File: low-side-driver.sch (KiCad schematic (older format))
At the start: 4 parts, among them U2 74HC595

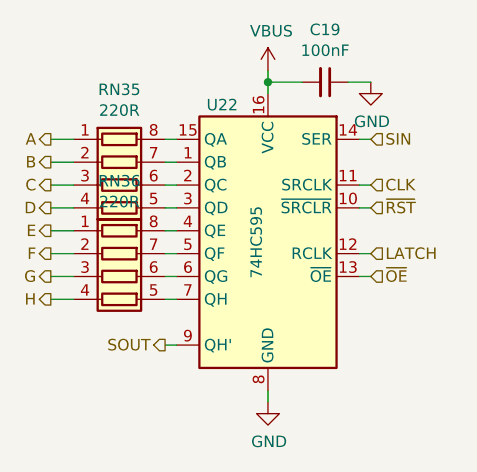
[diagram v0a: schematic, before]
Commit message: Use better ESP32 Pico D4 footprint
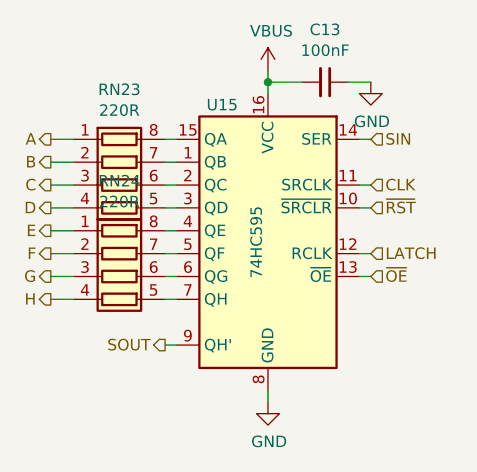
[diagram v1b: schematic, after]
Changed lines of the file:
@@
 $Descr A4 11693 8268
 encoding utf-8
-Sheet 5 25
+Sheet 16 25
 Title ""
 Date ""
@@
 AR Path="/61C4C905/61A75B6D/61A5FAFA" Ref="#PWR0153"  Part="1"
 AR Path="/61C4C905/61A75B93/61A5FAFA" Ref="#PWR0156"  Part="1"
-F 0 "#PWR0156" H 4900 3900 50  0001 C CNN
+F 0 "#PWR0138" H 4900 3900 50  0001 C CNN
 F 1 "GND" H 4905 3977 50  0000 C CNN
 F 2 "" H 4900 4150 50  0001 C CNN
@@
 AR Path="/61C4C905/61A75B6D/61A64A59" Ref="#PWR0154"  Part="1"
 AR Path="/61C4C905/61A75B93/61A64A59" Ref="#PWR0157"  Part="1"
-F 0 "#PWR0157" H 5350 2500 50  0001 C CNN
+F 0 "#PWR0139" H 5350 2500 50  0001 C CNN
 F 1 "GND" H 5355 2577 50  0000 C CNN
 F 2 "" H 5350 2750 50  0001 C CNN
@@
 AR Path="/61C4C905/61A75B6D/61A63F1A" Ref="C18"  Part="1"
 AR Path="/61C4C905/61A75B93/61A63F1A" Ref="C19"  Part="1"
-F 0 "C19" V 4921 2750 50  0000 C CNN
+F 0 "C13" V 4921 2750 50  0000 C CNN
 F 1 "100nF" V 5012 2750 50  0000 C CNN
 F 2 "Capacitor_SMD:C_0402_1005Metric" H 5150 2750 50  0001 C CNN
@@
 AR Path="/61C4C905/61A75B6D/61A5EC64" Ref="#PWR0155"  Part="1"
 AR Path="/61C4C905/61A75B93/61A5EC64" Ref="#PWR0158"  Part="1"
-F 0 "#PWR0158" H 4900 2550 50  0001 C CNN
+F 0 "#PWR0140" H 4900 2550 50  0001 C CNN
 F 1 "VBUS" H 4915 2873 50  0000 C CNN
 F 2 "" H 4900 2700 50  0001 C CNN
@@
 AR Path="/61C4C905/61A75B6D/61A5E6B7" Ref="RN34"  Part="1"
 AR Path="/61C4C905/61A75B93/61A5E6B7" Ref="RN36"  Part="1"
-F 0 "RN36" V 3833 3600 50  0000 C CNN
+F 0 "RN24" V 3833 3600 50  0000 C CNN
 F 1 "220R" V 3924 3600 50  0000 C CNN
 F 2 "Resistor_SMD:R_Array_Concave_4x0402" V 4525 3600 50  0001 C CNN
@@
 AR Path="/61C4C905/61A75B6D/61A5E6AC" Ref="RN33"  Part="1"
 AR Path="/61C4C905/61A75B93/61A5E6AC" Ref="RN35"  Part="1"
-F 0 "RN35" V 3833 3200 50  0000 C CNN
+F 0 "RN23" V 3833 3200 50  0000 C CNN
 F 1 "220R" V 3924 3200 50  0000 C CNN
 F 2 "Resistor_SMD:R_Array_Concave_4x0402" V 4525 3200 50  0001 C CNN
@@
 AR Path="/61C4C905/61A75B6D/61A5E6A5" Ref="U21"  Part="1"
 AR Path="/61C4C905/61A75B93/61A5E6A5" Ref="U22"  Part="1"
-F 0 "U22" H 5100 3950 50  0000 C CNN
+F 0 "U15" H 5100 3950 50  0000 C CNN
 F 1 "74HC595" V 4950 3350 50  0000 C CNN
 F 2 "Package_Texas:X1QFN-16-2.5x2.5-EP-1.2" H 4900 3400 50  0001 C CNN

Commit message: Add additional VBUS bulk capacitance
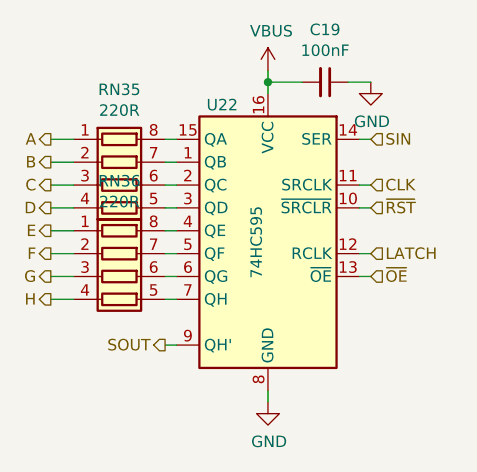
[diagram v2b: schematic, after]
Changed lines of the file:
@@
 $Descr A4 11693 8268
 encoding utf-8
-Sheet 16 25
+Sheet 21 25
 Title ""
 Date ""
@@
 AR Path="/61C4C905/61A75B6D/61A5FAFA" Ref="#PWR0153"  Part="1"
 AR Path="/61C4C905/61A75B93/61A5FAFA" Ref="#PWR0156"  Part="1"
-F 0 "#PWR0138" H 4900 3900 50  0001 C CNN
+F 0 "#PWR0156" H 4900 3900 50  0001 C CNN
 F 1 "GND" H 4905 3977 50  0000 C CNN
 F 2 "" H 4900 4150 50  0001 C CNN
@@
 AR Path="/61C4C905/61A75B6D/61A64A59" Ref="#PWR0154"  Part="1"
 AR Path="/61C4C905/61A75B93/61A64A59" Ref="#PWR0157"  Part="1"
-F 0 "#PWR0139" H 5350 2500 50  0001 C CNN
+F 0 "#PWR0157" H 5350 2500 50  0001 C CNN
 F 1 "GND" H 5355 2577 50  0000 C CNN
 F 2 "" H 5350 2750 50  0001 C CNN
@@
 AR Path="/61C4C905/61A75B6D/61A63F1A" Ref="C18"  Part="1"
 AR Path="/61C4C905/61A75B93/61A63F1A" Ref="C19"  Part="1"
-F 0 "C13" V 4921 2750 50  0000 C CNN
+F 0 "C19" V 4921 2750 50  0000 C CNN
 F 1 "100nF" V 5012 2750 50  0000 C CNN
 F 2 "Capacitor_SMD:C_0402_1005Metric" H 5150 2750 50  0001 C CNN
@@
 AR Path="/61C4C905/61A75B6D/61A5EC64" Ref="#PWR0155"  Part="1"
 AR Path="/61C4C905/61A75B93/61A5EC64" Ref="#PWR0158"  Part="1"
-F 0 "#PWR0140" H 4900 2550 50  0001 C CNN
+F 0 "#PWR0158" H 4900 2550 50  0001 C CNN
 F 1 "VBUS" H 4915 2873 50  0000 C CNN
 F 2 "" H 4900 2700 50  0001 C CNN
@@
 AR Path="/61C4C905/61A75B6D/61A5E6B7" Ref="RN34"  Part="1"
 AR Path="/61C4C905/61A75B93/61A5E6B7" Ref="RN36"  Part="1"
-F 0 "RN24" V 3833 3600 50  0000 C CNN
+F 0 "RN36" V 3833 3600 50  0000 C CNN
 F 1 "220R" V 3924 3600 50  0000 C CNN
 F 2 "Resistor_SMD:R_Array_Concave_4x0402" V 4525 3600 50  0001 C CNN
@@
 AR Path="/61C4C905/61A75B6D/61A5E6AC" Ref="RN33"  Part="1"
 AR Path="/61C4C905/61A75B93/61A5E6AC" Ref="RN35"  Part="1"
-F 0 "RN23" V 3833 3200 50  0000 C CNN
+F 0 "RN35" V 3833 3200 50  0000 C CNN
 F 1 "220R" V 3924 3200 50  0000 C CNN
 F 2 "Resistor_SMD:R_Array_Concave_4x0402" V 4525 3200 50  0001 C CNN
@@
 AR Path="/61C4C905/61A75B6D/61A5E6A5" Ref="U21"  Part="1"
 AR Path="/61C4C905/61A75B93/61A5E6A5" Ref="U22"  Part="1"
-F 0 "U15" H 5100 3950 50  0000 C CNN
+F 0 "U22" H 5100 3950 50  0000 C CNN
 F 1 "74HC595" V 4950 3350 50  0000 C CNN
 F 2 "Package_Texas:X1QFN-16-2.5x2.5-EP-1.2" H 4900 3400 50  0001 C CNN

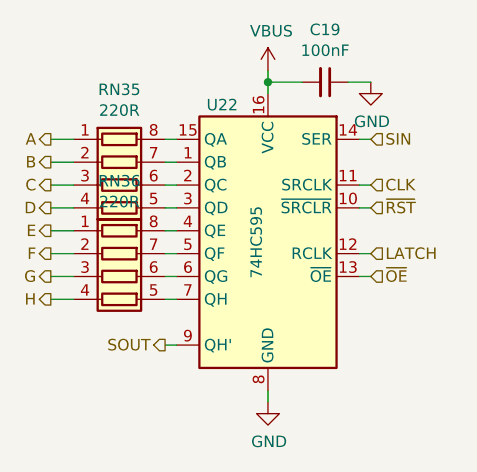
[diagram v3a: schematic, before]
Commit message: Add missing part references
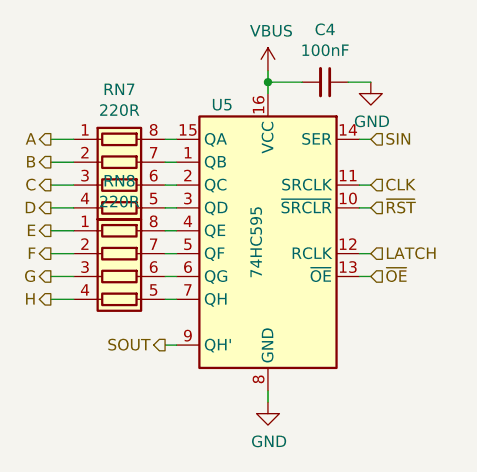
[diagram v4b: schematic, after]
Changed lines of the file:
@@
 $Descr A4 11693 8268
 encoding utf-8
-Sheet 7 25
+Sheet 6 25
 Title ""
 Date ""
@@
 AR Path="/61C4C905/61A75B6D/61A5FAFA" Ref="#PWR0153"  Part="1"
 AR Path="/61C4C905/61A75B93/61A5FAFA" Ref="#PWR0156"  Part="1"
-F 0 "#PWR0156" H 4900 3900 50  0001 C CNN
+F 0 "#PWR0110" H 4900 3900 50  0001 C CNN
 F 1 "GND" H 4905 3977 50  0000 C CNN
 F 2 "" H 4900 4150 50  0001 C CNN
@@
 AR Path="/61C4C905/61A75B6D/61A64A59" Ref="#PWR0154"  Part="1"
 AR Path="/61C4C905/61A75B93/61A64A59" Ref="#PWR0157"  Part="1"
-F 0 "#PWR0157" H 5350 2500 50  0001 C CNN
+F 0 "#PWR0111" H 5350 2500 50  0001 C CNN
 F 1 "GND" H 5355 2577 50  0000 C CNN
 F 2 "" H 5350 2750 50  0001 C CNN
@@
 AR Path="/61C4C905/61A75B6D/61A63F1A" Ref="C18"  Part="1"
 AR Path="/61C4C905/61A75B93/61A63F1A" Ref="C19"  Part="1"
-F 0 "C19" V 4921 2750 50  0000 C CNN
+F 0 "C4" V 4921 2750 50  0000 C CNN
 F 1 "100nF" V 5012 2750 50  0000 C CNN
 F 2 "Capacitor_SMD:C_0402_1005Metric" H 5150 2750 50  0001 C CNN
@@
 AR Path="/61C4C905/61A75B6D/61A5EC64" Ref="#PWR0155"  Part="1"
 AR Path="/61C4C905/61A75B93/61A5EC64" Ref="#PWR0158"  Part="1"
-F 0 "#PWR0158" H 4900 2550 50  0001 C CNN
+F 0 "#PWR0112" H 4900 2550 50  0001 C CNN
 F 1 "VBUS" H 4915 2873 50  0000 C CNN
 F 2 "" H 4900 2700 50  0001 C CNN
@@
 AR Path="/61C4C905/61A75B6D/61A5E6B7" Ref="RN34"  Part="1"
 AR Path="/61C4C905/61A75B93/61A5E6B7" Ref="RN36"  Part="1"
-F 0 "RN36" V 3833 3600 50  0000 C CNN
+F 0 "RN8" V 3833 3600 50  0000 C CNN
 F 1 "220R" V 3924 3600 50  0000 C CNN
 F 2 "Resistor_SMD:R_Array_Concave_4x0402" V 4525 3600 50  0001 C CNN
@@
 AR Path="/61C4C905/61A75B6D/61A5E6AC" Ref="RN33"  Part="1"
 AR Path="/61C4C905/61A75B93/61A5E6AC" Ref="RN35"  Part="1"
-F 0 "RN35" V 3833 3200 50  0000 C CNN
+F 0 "RN7" V 3833 3200 50  0000 C CNN
 F 1 "220R" V 3924 3200 50  0000 C CNN
 F 2 "Resistor_SMD:R_Array_Concave_4x0402" V 4525 3200 50  0001 C CNN
@@
 AR Path="/61C4C905/61A75B6D/61A5E6A5" Ref="U21"  Part="1"
 AR Path="/61C4C905/61A75B93/61A5E6A5" Ref="U22"  Part="1"
-F 0 "U22" H 5100 3950 50  0000 C CNN
+F 0 "U5" H 5100 3950 50  0000 C CNN
 F 1 "74HC595" V 4950 3350 50  0000 C CNN
 F 2 "Package_Texas:X1QFN-16-2.5x2.5-EP-1.2" H 4900 3400 50  0001 C CNN
